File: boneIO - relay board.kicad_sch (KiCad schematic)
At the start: 91 parts, among them J1 Screw_Terminal_01x04, J10 Screw_Terminal_01x04, J11 Screw_Terminal_01x04, J12 Screw_Terminal_01x04, J13 Screw_Terminal_01x04, J2 Screw_Terminal_01x04, J3 Conn_02x04_Odd_Even, J4 Screw_Terminal_01x04, J5 Screw_Terminal_01x04, J6 Screw_Terminal_01x04, J7 Screw_Terminal_01x04, J8 Screw_Terminal_01x04, J9 Screw_Terminal_01x04, K1 RM85-2011-35-1024, K10 RM85-2011-35-1024, K11 RM85-2011-35-1024, K12 RM85-2011-35-1024, K13 RM85-2011-35-1024, K14 RM85-2011-35-1024, K15 RM85-2011-35-1024, K16 RM85-2011-35-1024, K17 RM85-2011-35-1024, K18 RM85-2011-35-1024, K19 RM85-2011-35-1024, K2 RM85-2011-35-1024, K20 RM85-2011-35-1024, K21 RM85-2011-35-1024, K22 RM85-2011-35-1024, K23 RM85-2011-35-1024, K24 RM85-2011-35-1024, K3 RM85-2011-35-1024, K4 RM85-2011-35-1024, K5 RM85-2011-35-1024, K6 RM85-2011-35-1024, K7 RM85-2011-35-1024, K8 RM85-2011-35-1024, K9 RM85-2011-35-1024, SW1 SW_DIP_x03, SW2 SW_DIP_x03, SW3 SW_DIP_x03, U1 MCP9808-E_SO8, U2 MCP9808-E_MS, U3 ULN2803A, U4 ULN2803A, U5 ULN2803A, U6 MCP23017_SS, U7 MCP23017_SS

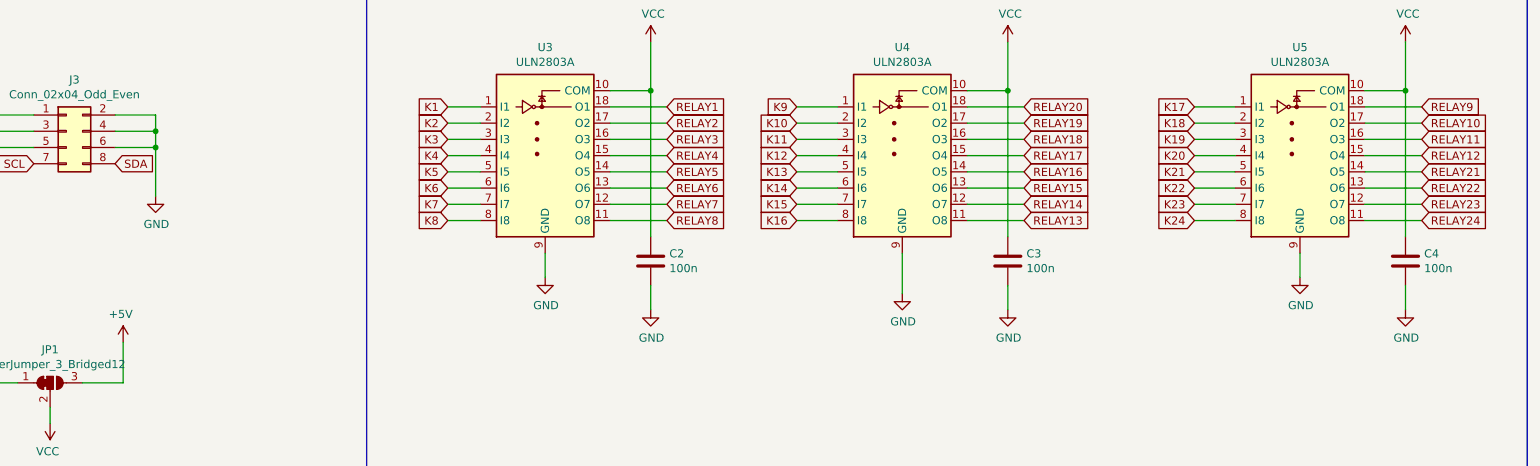
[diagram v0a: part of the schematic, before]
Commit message: relay board 24x16A v0.4 (rev2)
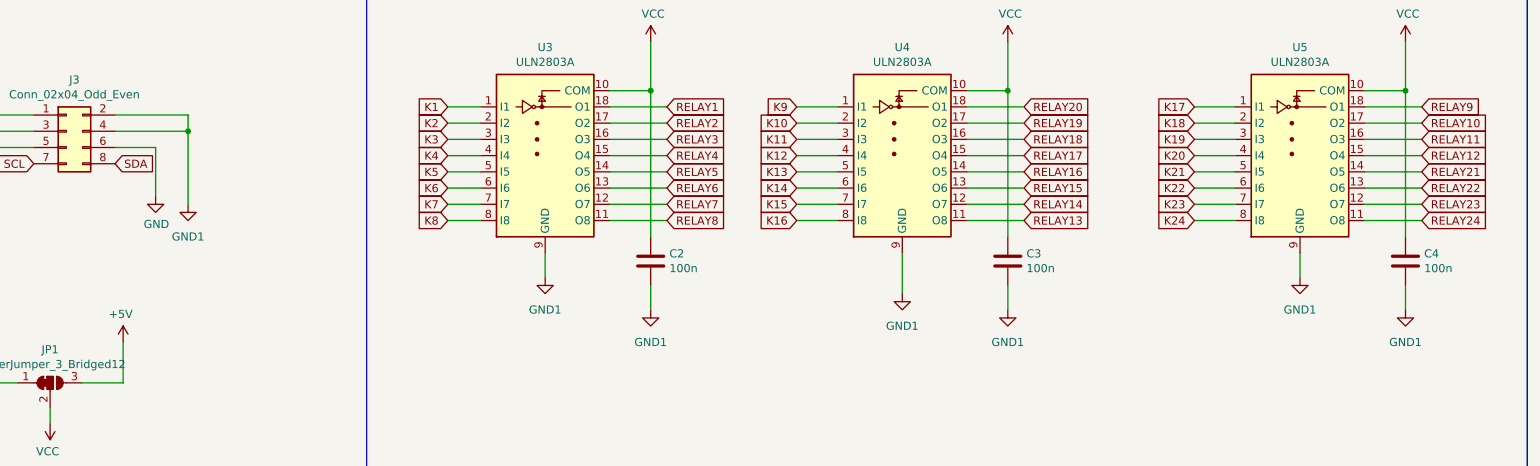
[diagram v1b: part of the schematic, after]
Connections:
- net GND: no longer C2.2, C3.2, C4.2, J3.2 (Pin_2), J3.4 (Pin_4), U3.9 (GND), U4.9 (GND), U5.9 (GND)
- new net GND1: C2.2, C3.2, C4.2, J3.2 (Pin_2), J3.4 (Pin_4), U3.9 (GND), U4.9 (GND), U5.9 (GND)
